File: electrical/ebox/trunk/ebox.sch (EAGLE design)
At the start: 161 parts, among them IC1 MAX3221CUE, IC10 SN74LVC1G125, IC11 MAX3221CUE, IC12 INA170, IC13 SN74LVC1G125, IC14 SN74LVC1G125, IC15 MAX3221CUE, IC16 MCP170333MB, IC17 SN74LVC1G125, IC18 SN74LVC1G125, IC19 74ALS04D, IC2 LT3652, IC3 XMEGA128A1, IC4 LT1161, IC5 SN74LVC1G125, IC6 SN74LVC1G125, IC7 MAX3221CUE, IC8 INA170, IC9 SN74LVC1G125, Q1 FDD4141TO252, U1 BLUETOOTH-RN42, U2 D2523T_, X1 7381-3PG-300, X10 DEANS-MALE, X11 B4B-ZR, X12 DEANS-MALE, X13 B4B-ZR, X14 22-23-2021, X15 DEANS-FEMALE, X16 DEANS-FEMALE, X17 USB_A, X18 22-23-2021, X2 7381-3PG-300, X3 7381-2PG-300, X4 17984-7PG-300, X5 17984-7PG-300, X6 17984-7PG-300, X7 17984-7PG-300, X8 22-23-2031, X9 22-23-2031

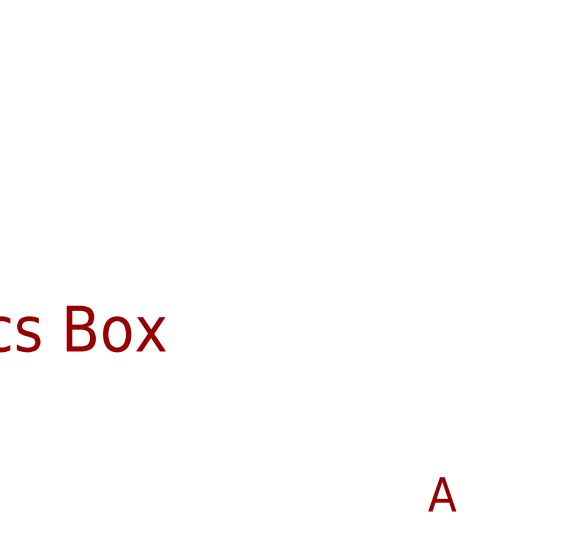
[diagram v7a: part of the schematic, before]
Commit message: Silkscreening complete.  Prepped for DFM check.
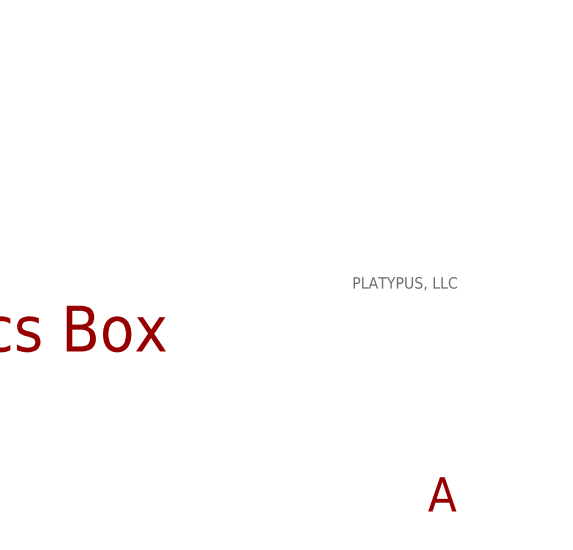
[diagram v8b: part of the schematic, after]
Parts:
- added U$1: PLATYPUS_LOGO, crw:PLATYPUS_LOGO
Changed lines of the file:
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@@
 <setting verticaltext="up"/>
 </settings>
-<grid distance="0.1" unitdist="inch" unit="inch" style="lines" multiple="1" display="yes" altdistance="0.01" altunitdist="inch" altunit="inch"/>
+<grid distance="0.1" unitdist="inch" unit="inch" style="lines" multiple="1" display="no" altdistance="0.01" altunitdist="inch" altunit="inch"/>
 <layers>
 <layer number="1" name="Top" color="4" fill="1" visible="no" active="no"/>
@@
 <part name="SUPPLY54" library="supply2" deviceset="GND" device=""/>
 <part name="R32" library="rcl" deviceset="R-US_" device="R0805" value="1K"/>
+<part name="U$1" library="crw" deviceset="PLATYPUS_LOGO" device=""/>
 </parts>
 <sheets>
@@
 <attribute name="VALUE" x="142.24" y="378.46" size="1.778" layer="96"/>
 </instance>
+<instance part="U$1" gate="G$1" x="546.1" y="33.02"/>
 </instances>
 <busses>
